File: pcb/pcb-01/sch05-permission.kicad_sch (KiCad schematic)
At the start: 0 parts

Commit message: pcb: capture SCH-04..07, full-project ERC clean
Parallel agent capture of the remaining blocks: SCH-04 ESP32-C6 (full GPIO
map, boot straps, USB chain with TPD2EUSB30 on the connector side of the
22R), SCH-05 permission + watchdog (both '1G74s with the review-fixed /PRE
topologies, six-BAT54H wired-OR, TPS3435 pinout C, separate 100R heartbeat
feeds), SCH-06 analog tach (TPS7A16 protected rail with 10 nF DELAY, LM2907
with grounded CP1 and emitter load, TLV1701 trip stage with C2 DNP ladder),
SCH-07 connectors J1-J8 + 28 test points + DNP input-fuse footprint.

ERC: 0 errors after PWR_FLAGs on VM24/AGND/PGND/TACH_LDO_IN and demoting
the MCF's duplicate OUTx/VM/PGND pins to passive. Konnect never refreshes a
sheet's embedded lib_symbols copy (delete + re-add reuses the stale def), so
that one fix was a keyword-only text edit of three pin types, verified by
kicad-cli's full parse. Remaining 41 warnings are two benign classes:
local+global same-name labels (our labeling convention) and embedded-vs-
library symbol formatting drift.

Vendored Konnect agents re-pinned from dead claude-sonnet-4-20250514 to
claude-sonnet-5.
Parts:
- added C22, C24, C25: 100nF, Capacitor_SMD:C_0402_1005Metric, symbol Device:C
- added C23: 10uF, Capacitor_SMD:C_0805_2012Metric, symbol Device:C
- added D3, D4, D5, D6, D7, D8: BAT54H, Diode_SMD:D_SOD-123, symbol Device:D_Schottky
- added Q2: 2N7002K, Package_TO_SOT_SMD:SOT-23, symbol Transistor_FET:2N7002K
- added R24, R36, R38: 100R, Resistor_SMD:R_0402_1005Metric, symbol Device:R
- added R25, R27, R31: 100k, Resistor_SMD:R_0402_1005Metric, symbol Device:R
- added R26: 1k, Resistor_SMD:R_0402_1005Metric, symbol Device:R
- added R28: 4.7k, Resistor_SMD:R_0402_1005Metric, symbol Device:R
- added R29, R30, R32, R33, R34, R35, R37: 10k, Resistor_SMD:R_0402_1005Metric, symbol Device:R
- added SW3: SW_Push, Button_Switch_SMD:SW_SPST_PTS645Sx43SMTR92, symbol Switch:SW_Push
- added U10, U11: SN74LVC1G17DCKR, Package_TO_SOT_SMD:SOT-353_SC-70-5, symbol 74xGxx:74LVC1G17
- added U5, U6: SN74LVC1G74DCTR, symbol 74xGxx:74AUP1G74
- added U7: TPS3435CAKAGDD, Package_TO_SOT_SMD:SOT-23-8, symbol pcb01-parts:TPS3435CAKAGDD
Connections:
- new net 3V3: C22.1, C24.1, C25.1, R29.1, R30.1, R31.1, R34.1, R35.1, R37.1, U10.5 (VCC), U11.5 (VCC), U5.2 (D), U5.7 (~{PRE}), U5.8 (VCC), U6.2 (D), U6.8 (VCC), U7.8 (VDD)
- new net AGND: C22.2, C23.2, C24.2, C25.2, Q2.2 (S), R25.2, R27.2, R32.2, R33.2, SW3.2, U10.3 (GND), U11.3 (GND), U5.4 (GND), U6.1 (C), U6.4 (GND), U7.4 (GND)
- new net ARM_PULSE: R24.1
- new net DRVOFF: Q2.3 (D), R28.2
- new net MCF_AVDD: R28.1
- new net MCF_EXT_WD: R38.2
- new net MCU_CLEAR_N: D6.1 (K)
- new net OS_LOCK_OK: D5.1 (K), U6.5 (Q)
- new net OVERSPEED_N: U6.6 (~{CLR})
- new net PGOOD: D3.1 (K), D8.1 (K)
- new net Q2_GATE: Q2.1 (G), R26.2, R27.1
- new net SET0: R32.1, U7.1 (SET0)
- new net SET1: R33.1, U7.5 (SET1)
- new net SW_CLR: D7.1 (K), R30.2, SW3.1
- new net U5_CLK: R24.2, R25.1, U5.1 (C)
- new net U5_CLR_BUF: U10.4, U5.6 (~{CLR})
- new net U5_CLR_OR: D3.2 (A), D4.2 (A), D5.2 (A), D6.2 (A), D7.2 (A), R29.2, U10.2
- new net U5_Q: R26.1, U5.5 (Q)
- new net U6_PRE_BUF: U11.4, U6.7 (~{PRE})
- new net U6_PRE_RC: C23.1, D8.2 (A), R31.2, U11.2
- new net U7_WDI: R36.2, U7.3 (WDI)
- new net WDO: D4.1 (K), R37.2, U7.7 (WDO)
- new net WD_EN: R35.2, U7.6 (WD-EN)
- new net WD_HEARTBEAT: R36.1, R38.1
- new net WD_MR: R34.2, U7.2 (MR)
- no-connect marks 0 -> 4

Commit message: pcb: custom footprints (MCF RGF, TPSM RDN, TI SM8) + full footprint assignment
pcb01-parts.pretty carries three datasheet-derived footprints: MCF8316D
VQFN-40 RGF0040E (40 pads + 3.7x5.7 EP + 12 POFV thermal vias at 0.3 mm
drill), TI SM8 DCT0008A with TI's 3.8 mm pad-row span (the number KiCad's
generic SSOP-8 gets wrong), and TPSM365R6 RDN0011A. The RDN pattern's
chained dimensions were ambiguous, so pad geometry was pixel-measured from
the 20X/600dpi render of TI drawing 4226623/F and cross-checked against the
direct labels; the VOUT/SW comb pads are simplified to rectangles at the
tooth-tip boundary (noted in the footprint description).

L1 uses KiCad's stock Sunlord SWPA6045S footprint. Every component now has
a footprint; ERC remains 0 errors with only the two known-benign warning
classes.
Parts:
- U5, U6: footprint (none) -> pcb01-parts:TI_SM8_DCT0008A
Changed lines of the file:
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@@
         (font
           (size 1.27 1.27))))
-    (property "Footprint" ""
+    (property "Footprint" "pcb01-parts:TI_SM8_DCT0008A"
       (at 85.09 49.53 0)
       (hide yes)
@@
         (font
           (size 1.27 1.27))))
-    (property "Footprint" ""
+    (property "Footprint" "pcb01-parts:TI_SM8_DCT0008A"
       (at 199.39 49.53 0)
       (hide yes)

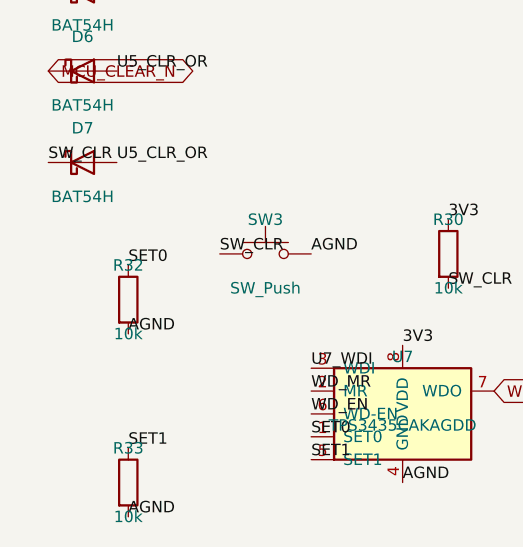
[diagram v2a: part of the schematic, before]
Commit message: pcb: review round 2 — safety-latch decoupling, docs, calibration rationale
Round-2 lenses (fix-verify, placement-physics, calibration math, MCF
register-image audit, completeness critic) confirmed every round-1 fix
end-to-end and found: U5 and U6 — the permission and overspeed latches —
were the only logic ICs without local decoupling (nearest 3V3 cap 13mm from
U5). Added C42/C43 (100nF 0402) on SCH-05. J5's stale MPN field corrected
to SM04B-SRSS-TB(LF)(SN).

Docs: calibration section now states WHY per-unit RV1 trim is mandatory
(LM2907 K = +/-10% => +/-20 RPM untrimmed) and the expected ~+/-10 RPM
threshold scatter (ripple ~= hysteresis) with the C36-C40 bank as the
remedy; open-items gains the MCF register-image capture checklist
(SPEED_MODE/SPEED_RANGE_SEL, ALARM_PIN_EN/OTW_REP, EXT_WDT_* and the
unmapped MAX_SPEED seed), the cold-plug VM ramp analysis (refuted by
bulk-bank physics, bench inrush check stands), and the V2 ESD note for
sensor pigtails/buttons. Verified: 12 thermal vias under U1's pad; zero new
wiring defects in the round-2 sweep; pole count, watchdog timing, trip
math all independently reproduce the documented targets.
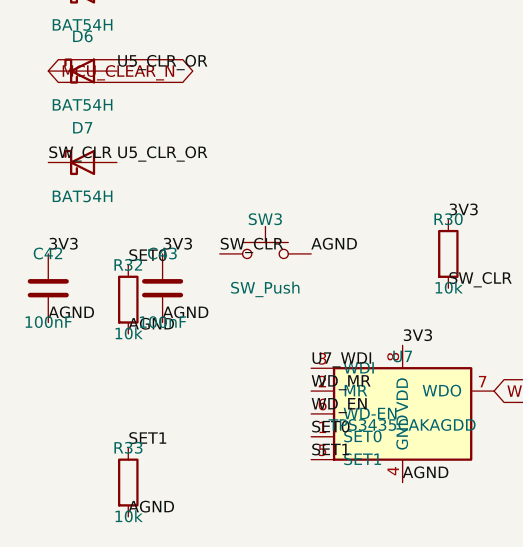
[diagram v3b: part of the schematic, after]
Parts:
- added C42, C43: 100nF, Capacitor_SMD:C_0402_1005Metric, symbol Device:C
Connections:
- net 3V3: now also C42.1, C43.1
- net AGND: now also C42.2, C43.2
